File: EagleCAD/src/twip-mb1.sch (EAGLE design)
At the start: 11 parts, among them U1 GY-521MPU6050

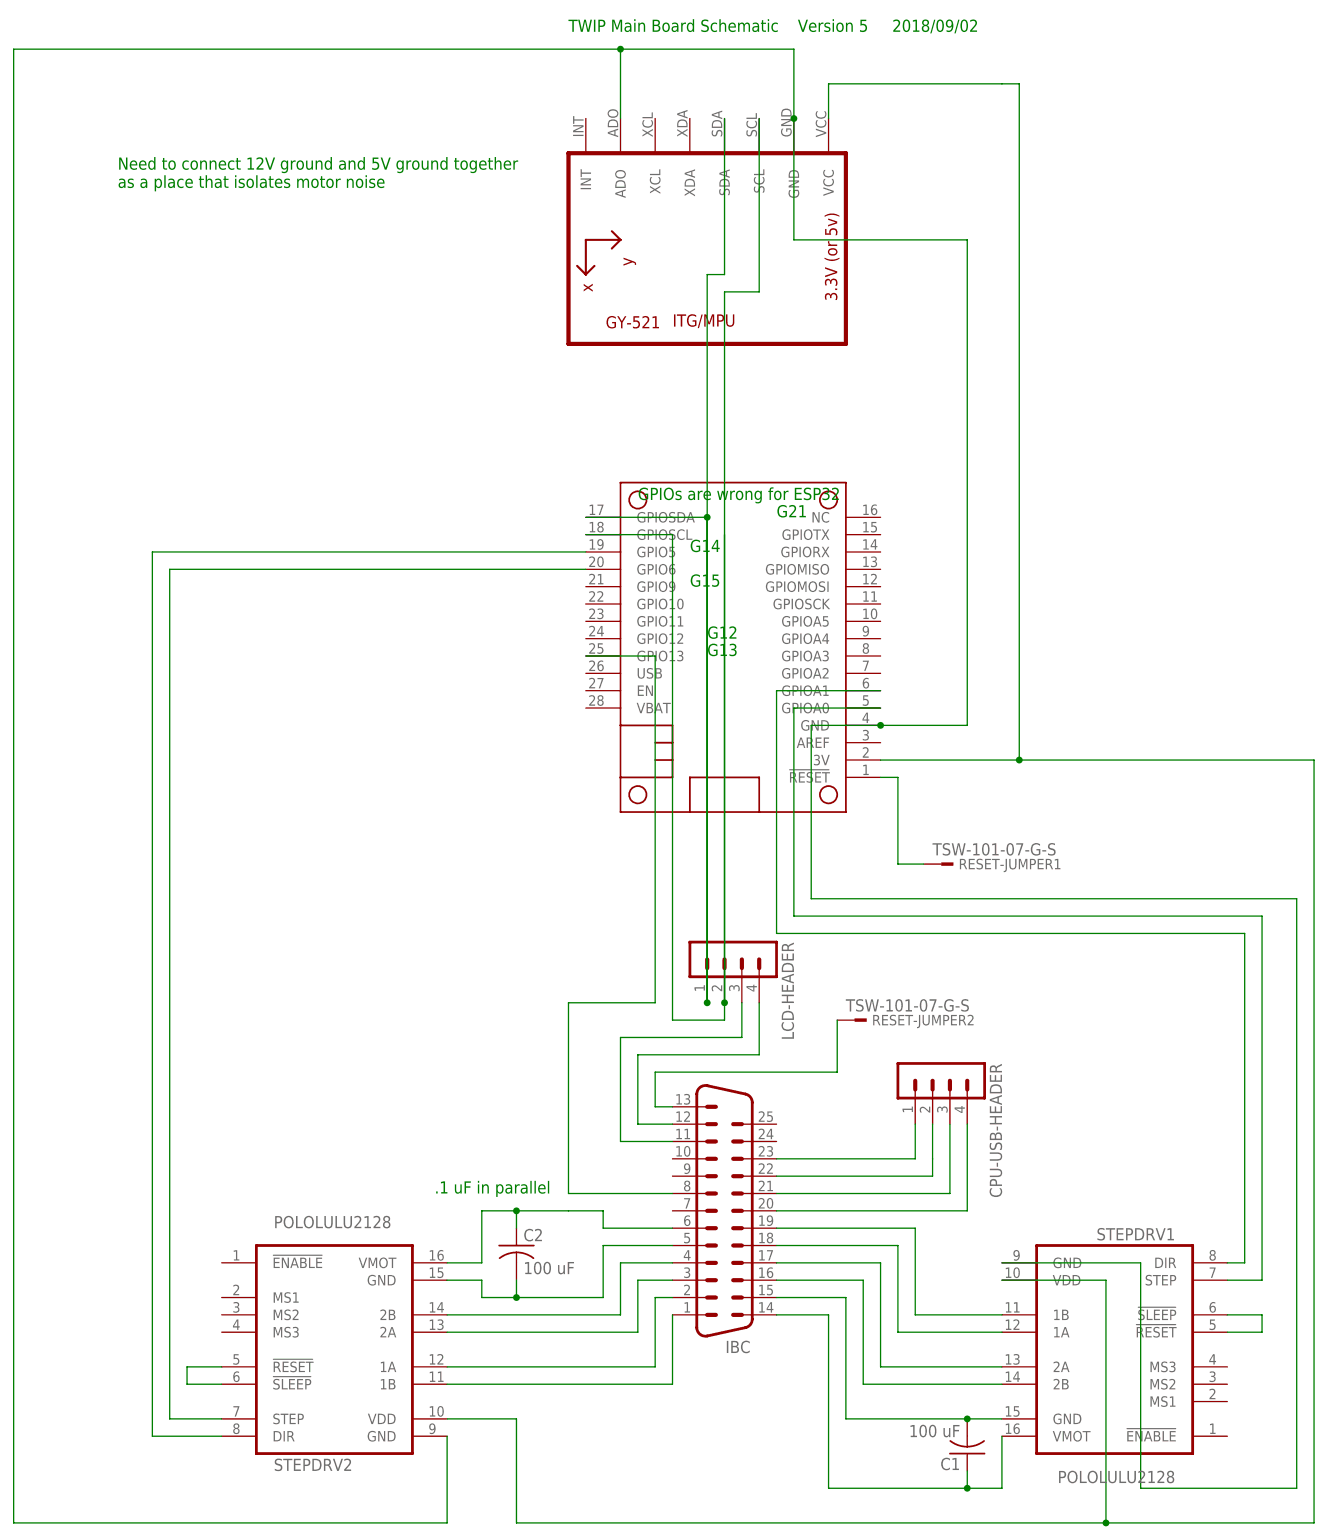
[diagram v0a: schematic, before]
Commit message: fix LCD header, as decoupling caps
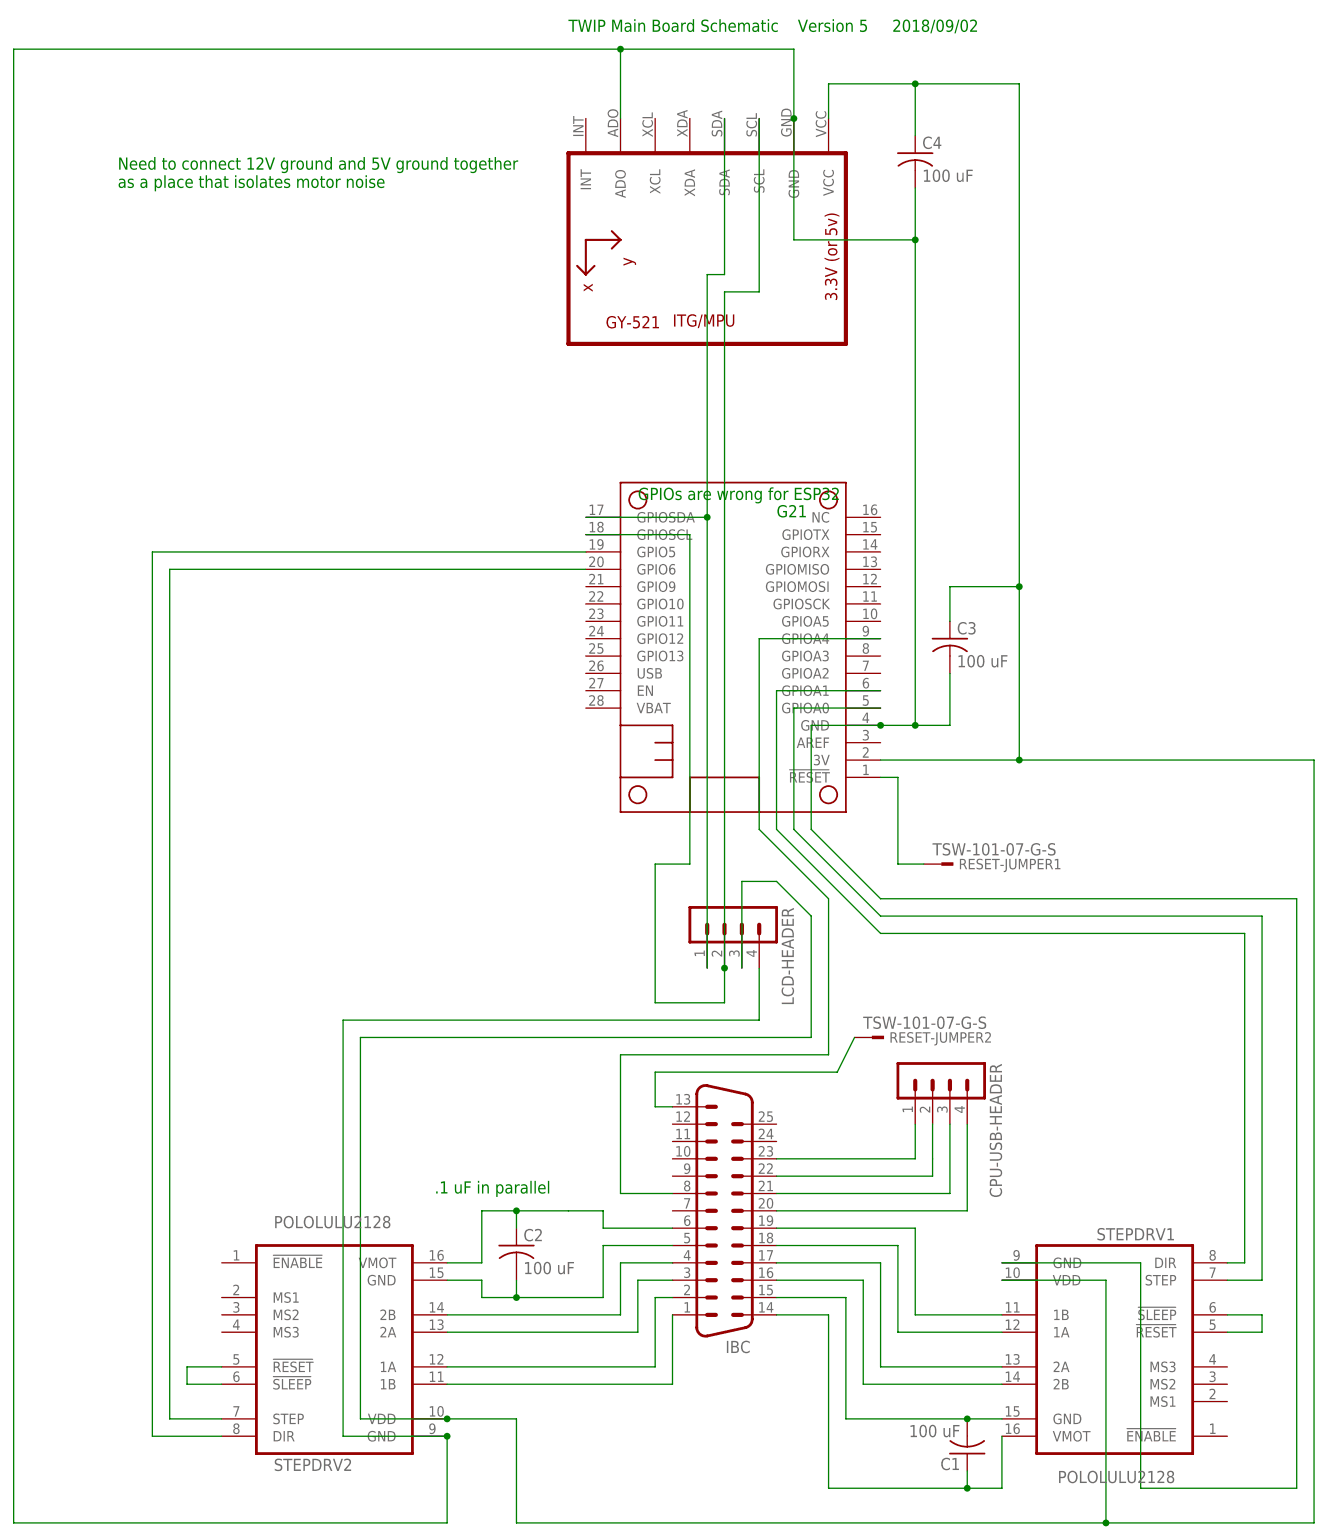
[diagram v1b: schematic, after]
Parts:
- added C3, C4: 100 uF, rcl:C-US025-024X044
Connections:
- removed net N$11 (its old number): IBCG$1.8, MS2.GPIO13
- removed net N$33: IBCG$1.11, LCD-HEADER.3
- removed net N$34: IBCG$1.12, LCD-HEADER.4
- new net N$28: IBCG$1.8, MS2.GPIOA4
- net 3V: now also C3.1, C4.1, LCD-HEADER.3
- net N$35: now also C3.2, C4.2, LCD-HEADER.4
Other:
- note removed: "G12"
- note removed: "G13"
- note removed: "G14"
- note removed: "G15"
- moved on the sheet: LCD-HEADER, RESET-JUMPER2

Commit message: Sep 24 checkpoint has mutually consistent versions of MB and PB layouts, and pinouts documentation
completed layout of peripheral board, with a few retrofits to MB for IBC connector changes. Added a 4 position DIP switch to PB as a way to have jumpers that cross other traces, as I couldn't quite do a single sided layout. All switches go to the right when active, and the voltage regulators, whose 4 legs are represented by two 5 pin headers, are correctly scaled. I'd like to space out the top connector for the stepper motor connections, but the board is at the max size allowed, and Eagle CAD won't allow it to be moved upward.
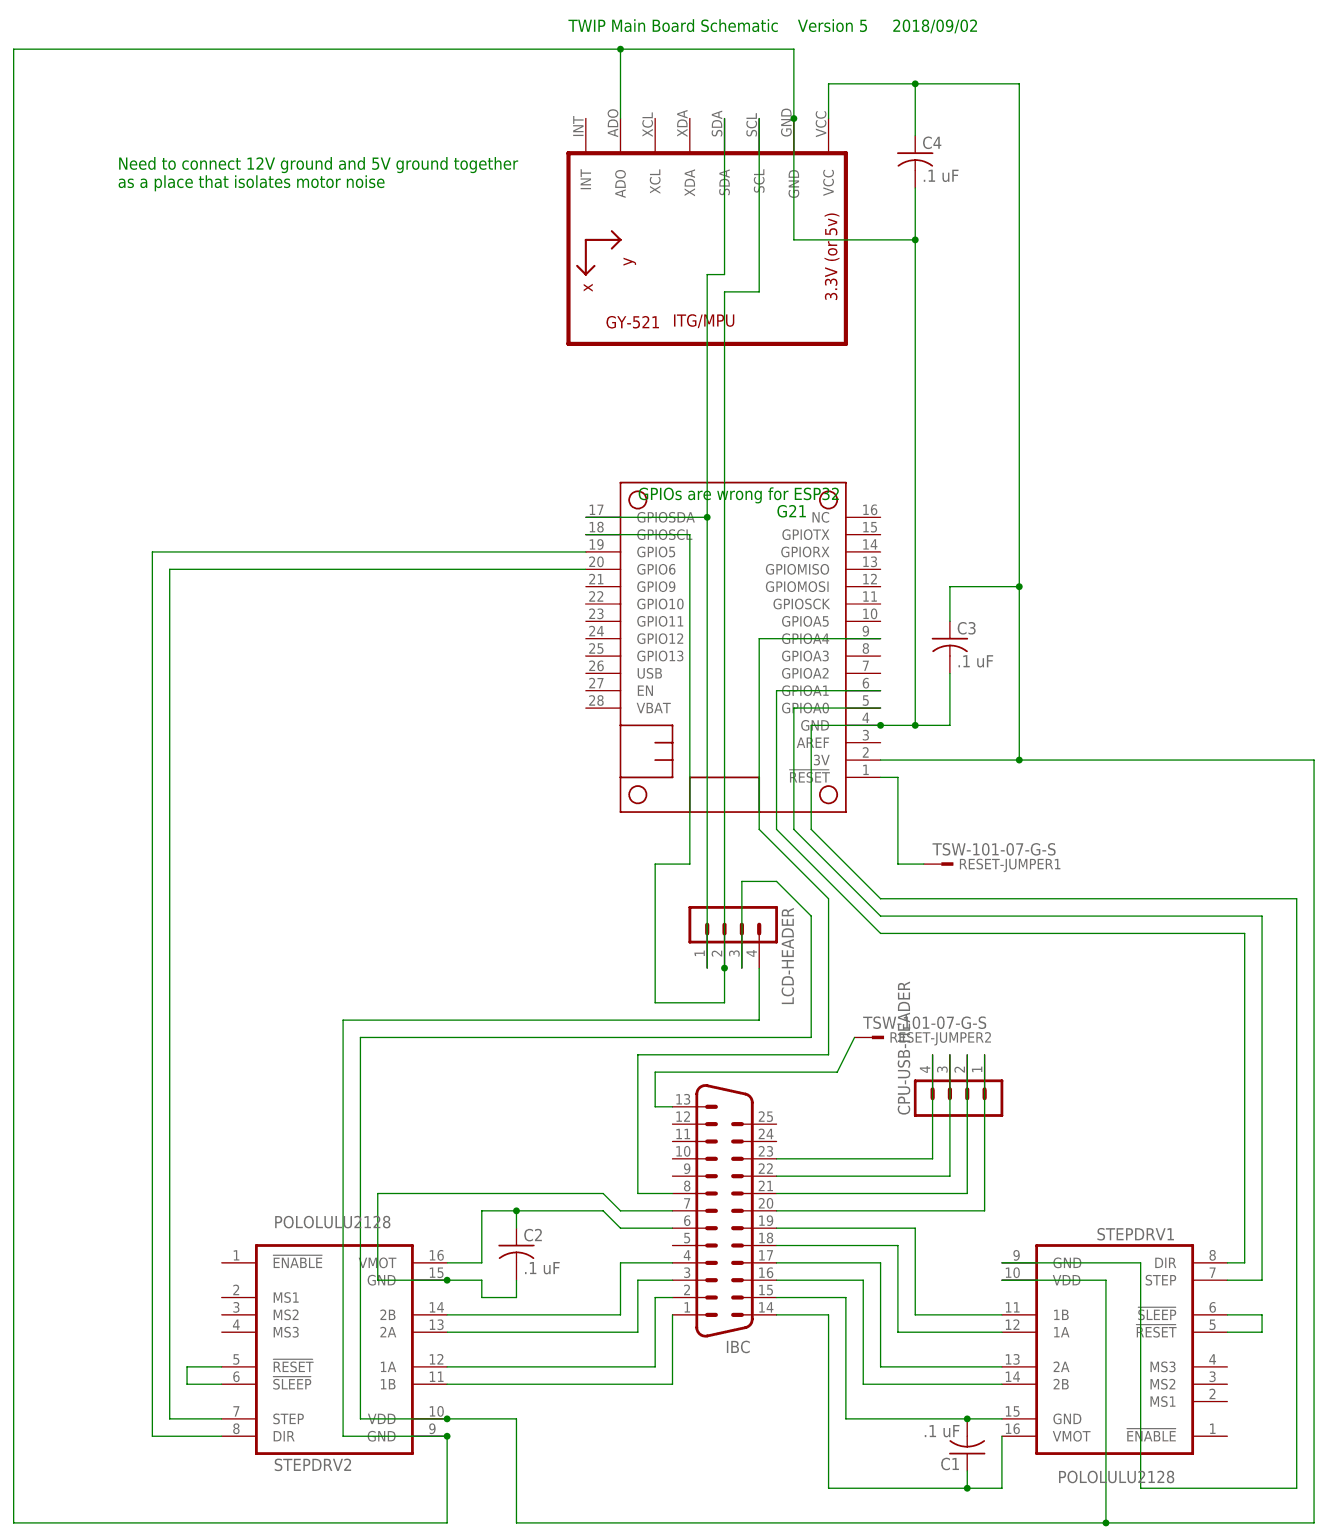
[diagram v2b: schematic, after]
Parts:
- C1, C2, C3, C4: value 100 uF -> .1 uF
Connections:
- net N$13: now also CPU-USB-HEADER.4; no longer CPU-USB-HEADER.1
- net N$14: now also CPU-USB-HEADER.3; no longer CPU-USB-HEADER.2
- net N$18: now also CPU-USB-HEADER.2; no longer CPU-USB-HEADER.3
- net N$2: now also IBCG$1.7; no longer IBCG$1.5
- net N$30: now also CPU-USB-HEADER.1; no longer CPU-USB-HEADER.4
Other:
- note removed: ".1 uF in parallel"
- moved on the sheet: CPU-USB-HEADER
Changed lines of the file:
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@@
 <part name="STEPDRV1" library="stepper_drivers_etc" deviceset="POLOLULU2128" device=""/>
 <part name="STEPDRV2" library="stepper_drivers_etc" deviceset="POLOLULU2128" device=""/>
-<part name="C1" library="rcl" library_urn="urn:adsk.eagle:library:334" deviceset="C-US" device="025-024X044" package3d_urn="urn:adsk.eagle:package:23630/1" value="100 uF"/>
-<part name="C2" library="rcl" library_urn="urn:adsk.eagle:library:334" deviceset="C-US" device="025-024X044" package3d_urn="urn:adsk.eagle:package:23630/1" value="100 uF"/>
+<part name="C1" library="rcl" library_urn="urn:adsk.eagle:library:334" deviceset="C-US" device="025-024X044" package3d_urn="urn:adsk.eagle:package:23630/1" value=".1 uF"/>
+<part name="C2" library="rcl" library_urn="urn:adsk.eagle:library:334" deviceset="C-US" device="025-024X044" package3d_urn="urn:adsk.eagle:package:23630/1" value=".1 uF"/>
 <part name="RESET-JUMPER2" library="con-samtec" library_urn="urn:adsk.eagle:library:184" deviceset="TSW-101-*-G-S" device="" technology="07"/>
 <part name="RESET-JUMPER1" library="con-samtec" library_urn="urn:adsk.eagle:library:184" deviceset="TSW-101-*-G-S" device="" technology="07"/>
 <part name="MS2" library="microbuilder" deviceset="FEATHERWING" device="_NOHOLES"/>
-<part name="C3" library="rcl" library_urn="urn:adsk.eagle:library:334" deviceset="C-US" device="025-024X044" package3d_urn="urn:adsk.eagle:package:23630/1" value="100 uF"/>
-<part name="C4" library="rcl" library_urn="urn:adsk.eagle:library:334" deviceset="C-US" device="025-024X044" package3d_urn="urn:adsk.eagle:package:23630/1" value="100 uF"/>
+<part name="C3" library="rcl" library_urn="urn:adsk.eagle:library:334" deviceset="C-US" device="025-024X044" package3d_urn="urn:adsk.eagle:package:23630/1" value=".1 uF"/>
+<part name="C4" library="rcl" library_urn="urn:adsk.eagle:library:334" deviceset="C-US" device="025-024X044" package3d_urn="urn:adsk.eagle:package:23630/1" value=".1 uF"/>
 </parts>
 <sheets>
@@
 as a place that isolates motor noise</text>
 <text x="109.22" y="220.98" size="1.778" layer="91">TWIP Main Board Schematic    Version 5     2018/09/02</text>
-<text x="88.9" y="50.8" size="1.778" layer="91"> .1 uF in parallel</text>
 </plain>
 <instances>
 <instance part="U1" gate="G$1" x="132.08" y="193.04" rot="R270"/>
 <instance part="LCD-HEADER" gate="1" x="134.62" y="91.44" rot="R270"/>
-<instance part="CPU-USB-HEADER" gate="1" x="165.1" y="68.58" rot="R270"/>
+<instance part="CPU-USB-HEADER" gate="1" x="165.1" y="63.5" rot="R90"/>
 <instance part="IBC" gate="G$1" x="132.08" y="45.72" rot="R180"/>
 <instance part="STEPDRV1" gate="G$1" x="190.5" y="27.94" rot="R180"/>
@@
 </segment>
 </net>
-<net name="N$17" class="0">
-<segment>
-<pinref part="STEPDRV2" gate="G$1" pin="VMOT"/>
-<wire x1="96.52" y1="48.26" x2="96.52" y2="40.64" width="0.1524" layer="91"/>
-<wire x1="96.52" y1="40.64" x2="91.44" y2="40.64" width="0.1524" layer="91"/>
-<wire x1="96.52" y1="48.26" x2="101.6" y2="48.26" width="0.1524" layer="91"/>
-<pinref part="C2" gate="G$1" pin="1"/>
-<wire x1="101.6" y1="48.26" x2="109.22" y2="48.26" width="0.1524" layer="91"/>
-<wire x1="101.6" y1="45.72" x2="101.6" y2="48.26" width="0.1524" layer="91"/>
-<junction x="101.6" y="48.26"/>
-<wire x1="109.22" y1="48.26" x2="114.3" y2="48.26" width="0.1524" layer="91"/>
-<wire x1="114.3" y1="48.26" x2="114.3" y2="45.72" width="0.1524" layer="91"/>
-<pinref part="IBC" gate="G$1" pin="6"/>
-<wire x1="114.3" y1="45.72" x2="124.46" y2="45.72" width="0.1524" layer="91"/>
-</segment>
-</net>
 <net name="N$16" class="0">
 <segment>
@@
 <pinref part="STEPDRV2" gate="G$1" pin="GND@0"/>
 <wire x1="91.44" y1="38.1" x2="96.52" y2="38.1" width="0.1524" layer="91"/>
-<wire x1="101.6" y1="35.56" x2="114.3" y2="35.56" width="0.1524" layer="91"/>
-<junction x="101.6" y="35.56"/>
-<wire x1="114.3" y1="35.56" x2="114.3" y2="43.18" width="0.1524" layer="91"/>
-<pinref part="IBC" gate="G$1" pin="5"/>
-<wire x1="114.3" y1="43.18" x2="124.46" y2="43.18" width="0.1524" layer="91"/>
+<wire x1="91.44" y1="38.1" x2="81.28" y2="38.1" width="0.1524" layer="91"/>
+<junction x="91.44" y="38.1"/>
+<wire x1="81.28" y1="38.1" x2="81.28" y2="50.8" width="0.1524" layer="91"/>
+<wire x1="81.28" y1="50.8" x2="114.3" y2="50.8" width="0.1524" layer="91"/>
+<wire x1="114.3" y1="50.8" x2="116.84" y2="48.26" width="0.1524" layer="91"/>
+<pinref part="IBC" gate="G$1" pin="7"/>
+<wire x1="116.84" y1="48.26" x2="124.46" y2="48.26" width="0.1524" layer="91"/>
 </segment>
 </net>
@@
 <segment>
 <pinref part="IBC" gate="G$1" pin="23"/>
-<wire x1="139.7" y1="55.88" x2="160.02" y2="55.88" width="0.1524" layer="91"/>
+<wire x1="139.7" y1="55.88" x2="162.56" y2="55.88" width="0.1524" layer="91"/>
+<pinref part="CPU-USB-HEADER" gate="1" pin="4"/>
+<wire x1="162.56" y1="71.12" x2="162.56" y2="55.88" width="0.1524" layer="91"/>
+</segment>
+</net>
+<net name="N$14" class="0">
+<segment>
+<pinref part="IBC" gate="G$1" pin="22"/>
+<wire x1="139.7" y1="53.34" x2="165.1" y2="53.34" width="0.1524" layer="91"/>
+<pinref part="CPU-USB-HEADER" gate="1" pin="3"/>
+<wire x1="165.1" y1="71.12" x2="165.1" y2="53.34" width="0.1524" layer="91"/>
+</segment>
+</net>
+<net name="N$18" class="0">
+<segment>
+<pinref part="IBC" gate="G$1" pin="21"/>
+<wire x1="139.7" y1="50.8" x2="167.64" y2="50.8" width="0.1524" layer="91"/>
+<pinref part="CPU-USB-HEADER" gate="1" pin="2"/>
+<wire x1="167.64" y1="71.12" x2="167.64" y2="50.8" width="0.1524" layer="91"/>
+</segment>
+</net>
+<net name="N$30" class="0">
+<segment>
+<pinref part="IBC" gate="G$1" pin="20"/>
+<wire x1="139.7" y1="48.26" x2="170.18" y2="48.26" width="0.1524" layer="91"/>
 <pinref part="CPU-USB-HEADER" gate="1" pin="1"/>
-<wire x1="160.02" y1="55.88" x2="160.02" y2="60.96" width="0.1524" layer="91"/>
-</segment>
-</net>
-<net name="N$14" class="0">
-<segment>
-<pinref part="IBC" gate="G$1" pin="22"/>
-<wire x1="139.7" y1="53.34" x2="162.56" y2="53.34" width="0.1524" layer="91"/>
-<wire x1="162.56" y1="53.34" x2="162.56" y2="55.88" width="0.1524" layer="91"/>
-<pinref part="CPU-USB-HEADER" gate="1" pin="2"/>
-<wire x1="162.56" y1="55.88" x2="162.56" y2="60.96" width="0.1524" layer="91"/>
-</segment>
-</net>
-<net name="N$18" class="0">
-<segment>
-<pinref part="IBC" gate="G$1" pin="21"/>
-<wire x1="139.7" y1="50.8" x2="165.1" y2="50.8" width="0.1524" layer="91"/>
-<pinref part="CPU-USB-HEADER" gate="1" pin="3"/>
-<wire x1="165.1" y1="50.8" x2="165.1" y2="60.96" width="0.1524" layer="91"/>
-</segment>
-</net>
-<net name="N$30" class="0">
-<segment>
-<pinref part="IBC" gate="G$1" pin="20"/>
-<wire x1="139.7" y1="48.26" x2="167.64" y2="48.26" width="0.1524" layer="91"/>
-<pinref part="CPU-USB-HEADER" gate="1" pin="4"/>
-<wire x1="167.64" y1="48.26" x2="167.64" y2="60.96" width="0.1524" layer="91"/>
+<wire x1="170.18" y1="71.12" x2="170.18" y2="48.26" width="0.1524" layer="91"/>
 </segment>
 </net>
@@
 <wire x1="137.16" y1="104.14" x2="147.32" y2="93.98" width="0.1524" layer="91"/>
 <wire x1="147.32" y1="93.98" x2="147.32" y2="71.12" width="0.1524" layer="91"/>
-<wire x1="116.84" y1="71.12" x2="147.32" y2="71.12" width="0.1524" layer="91"/>
+<wire x1="119.38" y1="71.12" x2="147.32" y2="71.12" width="0.1524" layer="91"/>
 <pinref part="IBC" gate="G$1" pin="8"/>
-<wire x1="124.46" y1="50.8" x2="116.84" y2="50.8" width="0.1524" layer="91"/>
-<wire x1="116.84" y1="50.8" x2="116.84" y2="71.12" width="0.1524" layer="91"/>
+<wire x1="124.46" y1="50.8" x2="119.38" y2="50.8" width="0.1524" layer="91"/>
+<wire x1="119.38" y1="50.8" x2="119.38" y2="71.12" width="0.1524" layer="91"/>
 </segment>
 </net>
@@
 </segment>
 </net>
+<net name="N$21" class="0">
+<segment>
+<pinref part="IBC" gate="G$1" pin="6"/>
+<pinref part="STEPDRV2" gate="G$1" pin="VMOT"/>
+<wire x1="116.84" y1="45.72" x2="124.46" y2="45.72" width="0.1524" layer="91"/>
+<wire x1="96.52" y1="48.26" x2="96.52" y2="40.64" width="0.1524" layer="91"/>
+<wire x1="96.52" y1="40.64" x2="91.44" y2="40.64" width="0.1524" layer="91"/>
+<wire x1="96.52" y1="48.26" x2="101.6" y2="48.26" width="0.1524" layer="91"/>
+<pinref part="C2" gate="G$1" pin="1"/>
+<wire x1="101.6" y1="48.26" x2="114.3" y2="48.26" width="0.1524" layer="91"/>
+<wire x1="101.6" y1="45.72" x2="101.6" y2="48.26" width="0.1524" layer="91"/>
+<junction x="101.6" y="48.26"/>
+<wire x1="116.84" y1="45.72" x2="114.3" y2="48.26" width="0.1524" layer="91"/>
+</segment>
+</net>
